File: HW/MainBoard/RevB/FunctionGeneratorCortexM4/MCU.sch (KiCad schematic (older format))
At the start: 10 parts, among them J3 Conn_02x06_Odd_Even, J4 Conn_01x06, J5 Conn_01x03, J6 Conn_02x04_Odd_Even, J7 Conn_02x07_Odd_Even, U2 SN74LVC1G3157DCKR, U6 STM32G474RET

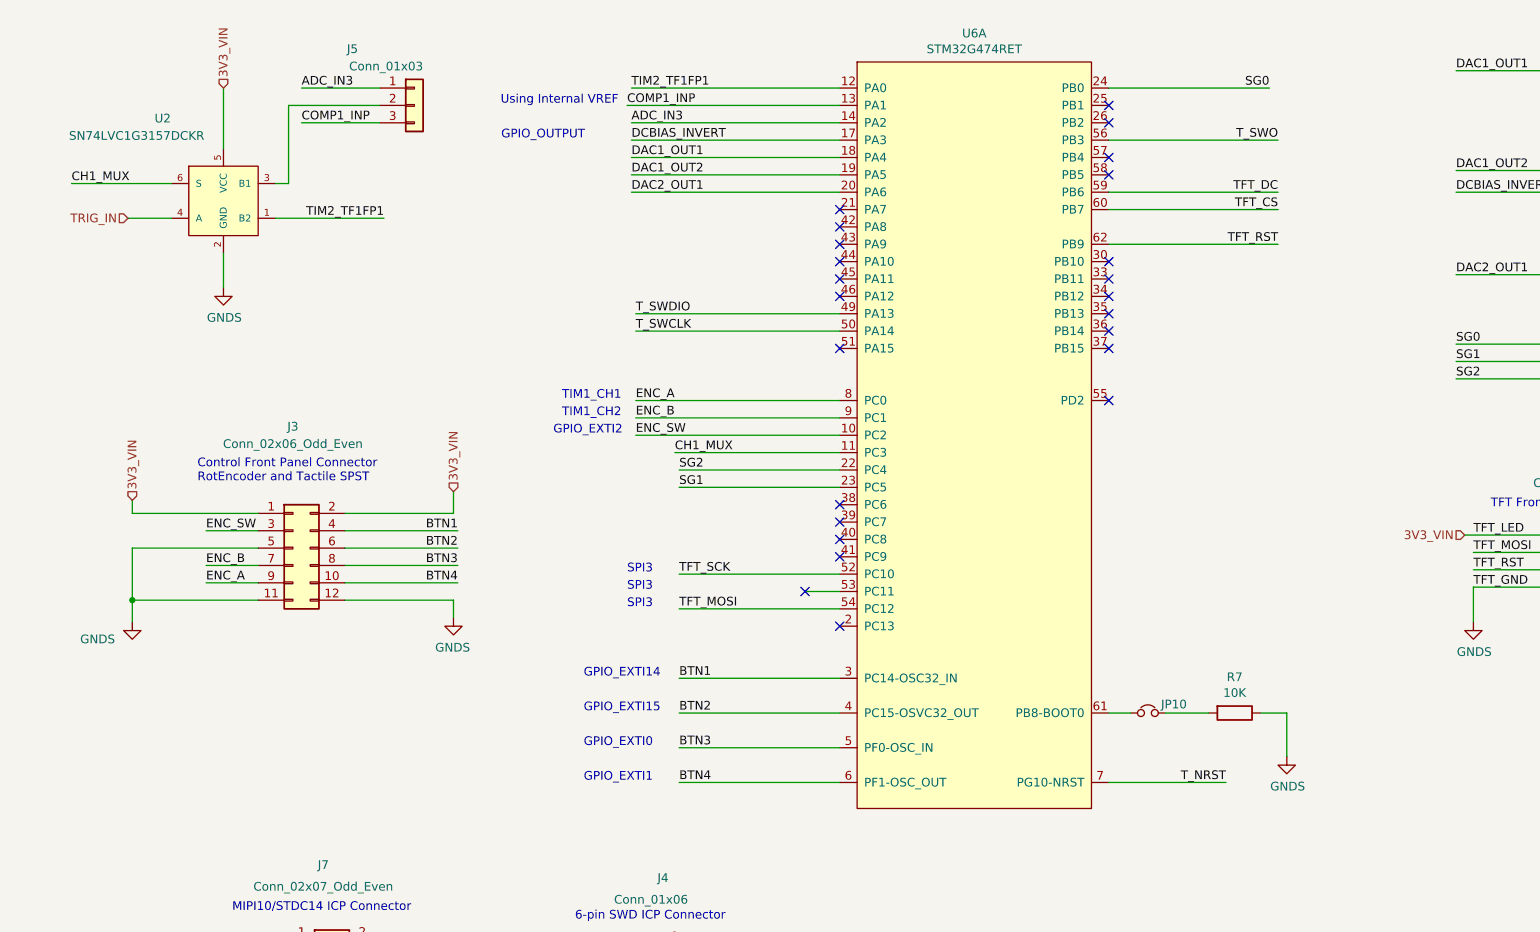
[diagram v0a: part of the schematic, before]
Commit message: REVB Update
- Changed TRIGIN J5 header to 2.54mm
- Changed IO J1 header to 2x05
- Added second charge pump IC
- Changed analog output circuit
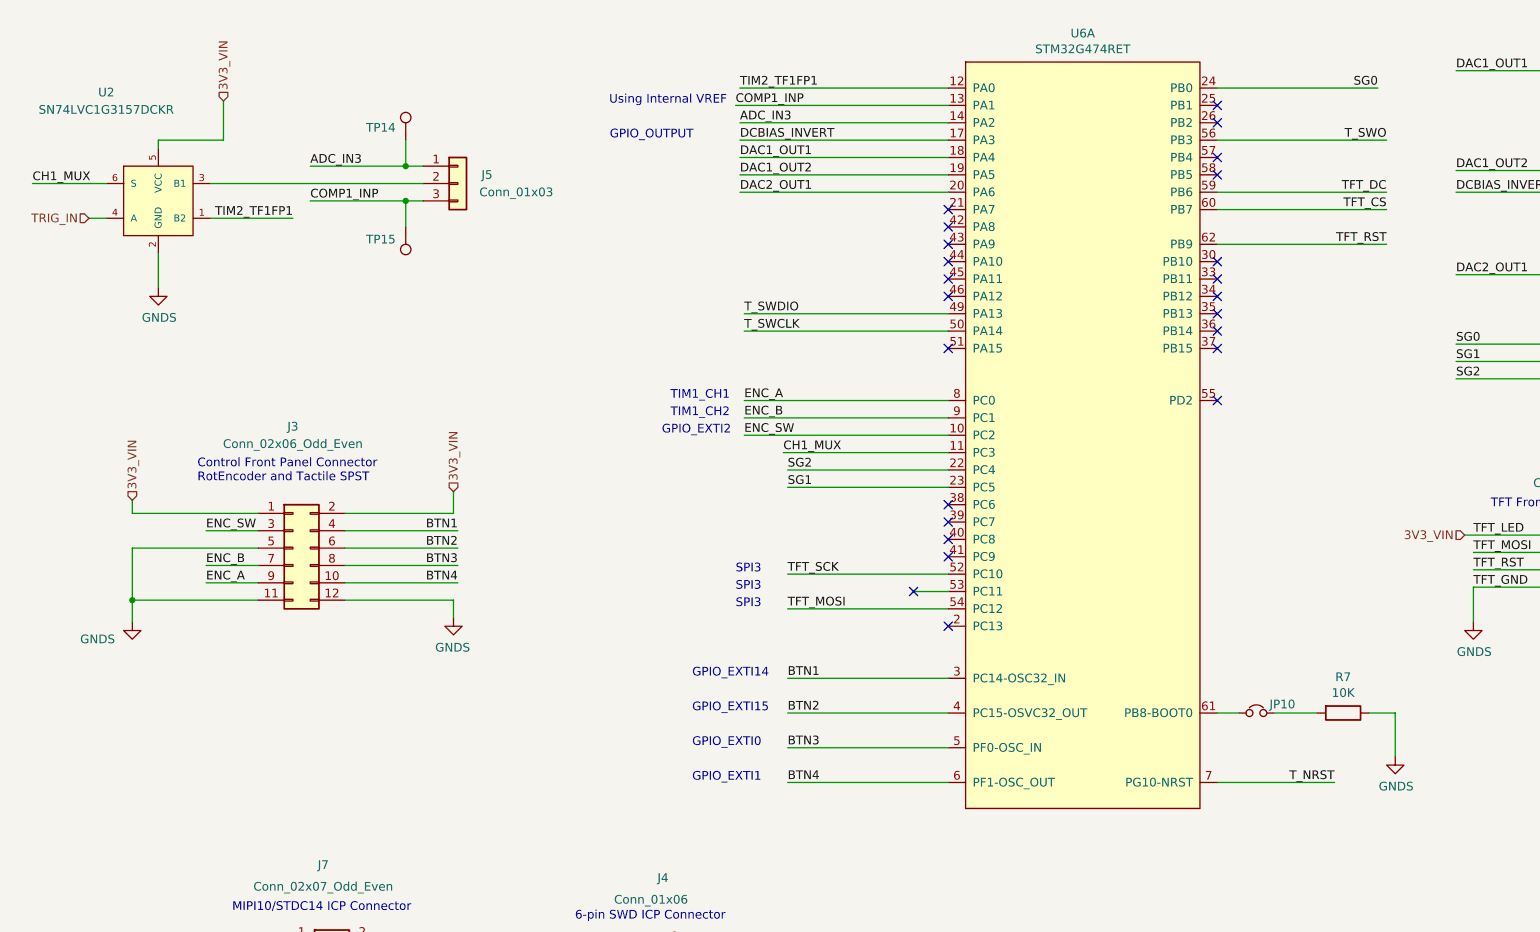
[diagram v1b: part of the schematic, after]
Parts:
- added TP14, TP15: TestPoint, TestPoint:TestPoint_Pad_1.0x1.0mm, symbol Connector:TestPoint
- J5: footprint Connector_PinHeader_1.27mm:PinHeader_1x03_P1.27mm_Vertical -> Connector_PinHeader_2.54mm:PinHeader_1x03_P2.54mm_Vertical
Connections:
- net ADC_IN3: now also TP14.1
- net COMP1_INP: now also TP15.1
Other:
- moved on the sheet: J5, JP10, R7, U2, U6A

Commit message: OPTIMIZED REVB LAYOUT
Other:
- moved on the sheet: J3, J4, J5, J6, J7, JP10, R11, R7, TP14, TP15, U2, U6A

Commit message: Final RevB Layout completed
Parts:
- removed J5: Conn_01x03, Connector_PinHeader_2.54mm:PinHeader_1x03_P2.54mm_Vertical, symbol Connector_Generic:Conn_01x03
- removed TP14, TP15: TestPoint, TestPoint:TestPoint_Pad_1.0x1.0mm, symbol Connector:TestPoint
- removed U2: SN74LVC1G3157DCKR, Package_TO_SOT_SMD:SOT-363_SC-70-6_Handsoldering, symbol SN74LVC1G3157:SN74LVC1G3157DCKR
- added C40: 100nF, Capacitor_SMD:C_0603_1608Metric_Pad1.05x0.95mm_HandSolder, symbol Device:C
- added U2: TS5A3357, Package_SO:VSSOP-8_2.4x2.1mm_P0.5mm, symbol TS5A3357:TS5A3357
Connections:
- net 3V3_VIN: now also C40.1, U2.8 (V+)
- net ADC_IN3: now also U2.3 (NO2)
- net COMP1_INP: now also U2.2 (NO1)
- net GNDS: now also C40.2, U2.4 (GND)
- net TIM2_TF1FP1: now also U2.1 (NO0)
- net TRIG_IN: now also U2.7 (COM)
- net TRIGMUX1: now reaches U6.40 (PC8)
- net TRIGMUX1: now also U2.6 (IN1)
- net TRIGMUX2: now reaches U6.41 (PC9)
- net TRIGMUX2: now also U2.5 (IN2)
- net CH1_MUX: no longer names the net of U6.11 (PC3)
- no-connect marks 30 -> 29
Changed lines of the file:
@@
 Text Label 6900 3400 0    50   ~ 0
 COMP1_INP
-Text Label 2900 2575 2    50   ~ 0
+Text Label 5150 2700 2    50   ~ 0
 TIM2_TF1FP1
-Wire Wire Line
-	2425 2575 2900 2575
-Text HLabel 2500 1900 1    50   Input ~ 0
+Text HLabel 3225 1675 1    50   Input ~ 0
 3V3_VIN
 $Comp
 L power:GNDS #PWR0113
 U 1 1 5EA1E126
-P 2125 2975
-F 0 "#PWR0113" H 2125 2725 50  0001 C CNN
-F 1 "GNDS" H 2130 2802 50  0000 C CNN
-F 2 "" H 2125 2975 50  0001 C CNN
-F 3 "" H 2125 2975 50  0001 C CNN
-	1    2125 2975
-	1    0    0    -1
-$EndComp
-Text HLabel 1725 2575 0    50   Input ~ 0
+P 3225 3775
+F 0 "#PWR0113" H 3225 3525 50  0001 C CNN
+F 1 "GNDS" H 3230 3602 50  0000 C CNN
+F 2 "" H 3225 3775 50  0001 C CNN
+F 3 "" H 3225 3775 50  0001 C CNN
+	1    3225 3775
+	1    0    0    -1
+$EndComp
+Text HLabel 1550 2700 0    50   Input ~ 0
 TRIG_IN
-Wire Wire Line
-	1825 2375 1400 2375
-Text Label 1400 2375 0    50   ~ 0
-CH1_MUX
 Text Notes 6850 3400 2    50   ~ 0
 Using Internal VREF
@@
 NoConn ~ 8125 4300
 NoConn ~ 8125 4800
-NoConn ~ 8125 5900
-NoConn ~ 8125 6000
 NoConn ~ 8125 6400
 NoConn ~ 9675 5100
@@
 Text Notes 13350 6850 0    50   ~ 0
 TFT Front Panel Display Connector
-$Comp
-L SN74LVC1G3157:SN74LVC1G3157DCKR U2
-U 1 1 5E6F0364
-P 2125 2475
-F 0 "U2" H 1825 3100 50  0000 C CNN
-F 1 "SN74LVC1G3157DCKR" H 1825 3000 50  0000 C CNN
-F 2 "Package_TO_SOT_SMD:SOT-363_SC-70-6_Handsoldering" H 1925 2175 50  0001 C CNN
-F 3 "http://www.ti.com/lit/ds/symlink/sn74lvc1g3157.pdf" H 2225 2675 50  0001 C CNN
-	1    2125 2475
-	1    0    0    -1
-$EndComp
-Wire Wire Line
-	2125 2975 2125 2775
-Wire Wire Line
-	1725 2575 1825 2575
+Wire Wire Line
+	1550 2700 2875 2700
 Wire Wire Line
 	7200 6300 8125 6300
@@
 GPIO_EXTI1
 Wire Wire Line
-	3000 2475 3550 2475
-Wire Wire Line
-	3000 2275 3550 2275
-Wire Wire Line
 	6925 3300 8125 3300
 Wire Wire Line
@@
 Text Label 6925 3600 0    50   ~ 0
 DCBIAS_INVERT
-Text Label 7175 5400 0    50   ~ 0
-CH1_MUX
-Wire Wire Line
-	7175 5400 8125 5400
 Text Notes 6900 6100 0    50   ~ 0
 SPI3
@@
 NoConn ~ 8125 4500
 NoConn ~ 8125 4100
-Text Label 3000 2275 0    50   ~ 0
+Text Label 5150 2900 2    50   ~ 0
 ADC_IN3
-Text Label 3000 2475 0    50   ~ 0
+Text Label 5150 2800 2    50   ~ 0
 COMP1_INP
-$Comp
-L Connector_Generic:Conn_01x03 J5
-U 1 1 5EDBA649
-P 3850 2375
-F 0 "J5" H 4050 2425 50  0000 R CNN
-F 1 "Conn_01x03" H 4400 2325 50  0000 R CNN
-F 2 "Connector_PinHeader_2.54mm:PinHeader_1x03_P2.54mm_Vertical" H 3850 2375 50  0001 C CNN
-F 3 "~" H 3850 2375 50  0001 C CNN
-	1    3850 2375
-	1    0    0    -1
-$EndComp
 Text Notes 6175 3600 0    50   ~ 0
 GPIO_OUTPUT
-Wire Wire Line
-	3550 2125 3550 2275
-Connection ~ 3550 2275
-Wire Wire Line
-	3550 2275 3650 2275
-Wire Wire Line
-	2425 2375 3650 2375
-$Comp
-L Connector:TestPoint TP?
-U 1 1 5F13C7D1
-P 3550 2625
-AR Path="/5E5FDE87/5F13C7D1" Ref="TP?"  Part="1"
-AR Path="/5E5FDD07/5F13C7D1" Ref="TP15"  Part="1"
-F 0 "TP15" H 3608 2697 50  0000 L CNN
-F 1 "TestPoint" H 3608 2652 50  0001 L CNN
-F 2 "TestPoint:TestPoint_Pad_1.0x1.0mm" H 3750 2625 50  0001 C CNN
-F 3 "~" H 3750 2625 50  0001 C CNN
-	1    3550 2625
-	-1   0    0    1
-$EndComp
-Wire Wire Line
-	3550 2625 3550 2475
-Connection ~ 3550 2475
-Wire Wire Line
-	3550 2475 3650 2475
-Wire Wire Line
-	2500 1900 2500 2125
-Wire Wire Line
-	2500 2125 2125 2125
-Wire Wire Line
-	2125 2125 2125 2175
-$Comp
-L Connector:TestPoint TP?
-U 1 1 5F0F3AA1
-P 3550 2125
-AR Path="/5E5FDE87/5F0F3AA1" Ref="TP?"  Part="1"
-AR Path="/5E5FDD07/5F0F3AA1" Ref="TP14"  Part="1"
-F 0 "TP14" H 3608 2197 50  0000 L CNN
-F 1 "TestPoint" H 3608 2152 50  0001 L CNN
-F 2 "TestPoint:TestPoint_Pad_1.0x1.0mm" H 3750 2125 50  0001 C CNN
-F 3 "~" H 3750 2125 50  0001 C CNN
-	1    3550 2125
-	-1   0    0    -1
-$EndComp
+$Comp
+L TS5A3357:TS5A3357 U2
+U 1 1 5EA3BED8
+P 3225 2850
+F 0 "U2" H 2925 3475 50  0000 C CNN
+F 1 "TS5A3357" H 2950 3400 50  0000 C CNN
+F 2 "Package_SO:VSSOP-8_2.4x2.1mm_P0.5mm" H 3175 2850 50  0001 C CNN
+F 3 "http://www.ti.com/lit/ds/symlink/ts5a3357.pdf" H 3175 2850 50  0001 C CNN
+	1    3225 2850
+	1    0    0    -1
+$EndComp
+Wire Wire Line
+	8125 5900 7200 5900
+Wire Wire Line
+	8125 6000 7200 6000
+Text Label 7200 5900 0    50   ~ 0
+TRIGMUX1
+Text Label 7200 6000 0    50   ~ 0
+TRIGMUX2
+Text Label 1675 2800 0    50   ~ 0
+TRIGMUX1
+Text Label 1675 2900 0    50   ~ 0
+TRIGMUX2
+NoConn ~ 8125 5400
+Wire Wire Line
+	1675 2900 2875 2900
+Wire Wire Line
+	1675 2800 2875 2800
+Wire Wire Line
+	3225 3250 3225 3775
+Wire Wire Line
+	3225 1800 3225 2350
+Wire Wire Line
+	3225 1675 3225 1800
+Connection ~ 3225 1800
+Wire Wire Line
+	2475 1800 3225 1800
+$Comp
+L power:GNDS #PWR0127
+U 1 1 5EB41EE5
+P 2475 2300
+F 0 "#PWR0127" H 2475 2050 50  0001 C CNN
+F 1 "GNDS" H 2480 2127 50  0000 C CNN
+F 2 "" H 2475 2300 50  0001 C CNN
+F 3 "" H 2475 2300 50  0001 C CNN
+	1    2475 2300
+	1    0    0    -1
+$EndComp
+Wire Wire Line
+	2475 1850 2475 1800
+Wire Wire Line
+	2475 2300 2475 2150
+$Comp
+L Device:C C40
+U 1 1 5EB3A3E6
+P 2475 2000
+F 0 "C40" H 2590 2046 50  0000 L CNN
+F 1 "100nF" H 2590 1955 50  0000 L CNN
+F 2 "Capacitor_SMD:C_0603_1608Metric_Pad1.05x0.95mm_HandSolder" H 2513 1850 50  0001 C CNN
+F 3 "~" H 2475 2000 50  0001 C CNN
+	1    2475 2000
+	1    0    0    -1
+$EndComp
+Wire Wire Line
+	3575 2700 5150 2700
+Wire Wire Line
+	3575 2800 5150 2800
+Wire Wire Line
+	3575 2900 5150 2900
 $EndSCHEMATC
